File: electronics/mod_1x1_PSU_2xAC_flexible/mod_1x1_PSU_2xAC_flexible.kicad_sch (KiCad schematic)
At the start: 56 parts, among them J1 module_2x15_left_input, J2 module_2x15_right_input, J3 Jack-DC, J4 Jack-DC, J5 Conn_01x02, J6 Conn_01x02, U1 LM317, U2 LM317, U3 LM337, U4 LM78XX

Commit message: updated PCB with newer/different footprints
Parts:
- removed D3, D4: D, SquantorDiodes:SOD-123F-hand, symbol Device:D
- removed R1: R, SquantorRcl:R_1206, symbol Device:R
- D10, D12, D14: footprint SquantorDiodes:SOD-523_hand -> SquantorDiodes:SOD-323-nexperia-hand
- N1: value 202200917 -> 202201025
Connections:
- net AC1_NEUT is gone; now on net GND: F2.2
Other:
- moved on the sheet: C1

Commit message: small changes for producability and form and fit
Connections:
- net +5V: now also J1.10 (+5V), J1.9 (+5V)
- net V+A: now also J2.3 (+VA), J2.4 (+VA)
- net V-A: now also J1.5 (-VA), J1.6 (-VA)
- no-connect marks 26 -> 20
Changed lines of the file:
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@@
   )
   (no_connect (at 38.1 50.8))
-  (no_connect (at 20.32 27.94))
   (no_connect (at 38.1 38.1))
   (no_connect (at 38.1 55.88))
   (no_connect (at 38.1 43.18))
   (no_connect (at 20.32 99.06))
-  (no_connect (at 20.32 73.66))
-  (no_connect (at 38.1 27.94))
   (no_connect (at 38.1 48.26))
   (no_connect (at 20.32 86.36))
   (no_connect (at 20.32 88.9))
-  (no_connect (at 20.32 33.02))
   (no_connect (at 38.1 40.64))
   (no_connect (at 20.32 104.14))
-  (no_connect (at 38.1 73.66))
   (no_connect (at 38.1 53.34))
   (no_connect (at 20.32 96.52))
@@
   (no_connect (at 90.17 134.62))
   (no_connect (at 20.32 101.6))
-  (no_connect (at 38.1 33.02))
   (wire (pts (xy 114.3 81.28) (xy 114.3 78.74))
     (stroke (width 0) (type default))
@@
     (stroke (width 0) (type default))
   )
+  (wire (pts (xy 38.1 73.66) (xy 40.64 73.66))
+    (stroke (width 0) (type default))
+  )
   (wire (pts (xy 113.03 76.2) (xy 114.3 76.2))
     (stroke (width 0) (type default))
@@
     (stroke (width 0) (type default))
   )
+  (wire (pts (xy 17.78 27.94) (xy 20.32 27.94))
+    (stroke (width 0) (type default))
+  )
   (wire (pts (xy 66.04 73.66) (xy 66.04 76.2))
     (stroke (width 0) (type default))
@@
     (stroke (width 0) (type default))
   )
+  (wire (pts (xy 38.1 27.94) (xy 40.64 27.94))
+    (stroke (width 0) (type default))
+  )
   (wire (pts (xy 19.05 50.8) (xy 20.32 50.8))
     (stroke (width 0) (type default))
@@
     (stroke (width 0) (type default))
   )
+  (wire (pts (xy 17.78 73.66) (xy 20.32 73.66))
+    (stroke (width 0) (type default))
+  )
   (polyline (pts (xy 46.99 151.13) (xy 72.39 151.13))
     (stroke (width 0) (type default))
@@
     (stroke (width 0) (type default))
   )
+  (wire (pts (xy 17.78 33.02) (xy 20.32 33.02))
+    (stroke (width 0) (type default))
+  )
   (wire (pts (xy 39.37 83.82) (xy 39.37 78.74))
     (stroke (width 0) (type default))
@@
     (stroke (width 0) (type default))
   )
+  (wire (pts (xy 38.1 33.02) (xy 40.64 33.02))
+    (stroke (width 0) (type default))
+  )
   (wire (pts (xy 58.42 16.51) (xy 58.42 21.59))
     (stroke (width 0) (type default))
@@
     (effects (font (size 1.27 1.27)) (justify left bottom))
   )
+  (label "+5V" (at 40.64 33.02 0) (fields_autoplaced)
+    (effects (font (size 1.27 1.27)) (justify left bottom))
+  )
   (label "DC1n" (at 102.87 83.82 0) (fields_autoplaced)
     (effects (font (size 1.27 1.27)) (justify left bottom))
@@
     (effects (font (size 1.27 1.27)) (justify left bottom))
   )
+  (label "V+A" (at 17.78 73.66 180) (fields_autoplaced)
+    (effects (font (size 1.27 1.27)) (justify right bottom))
+  )
   (label "V-A" (at 102.87 86.36 0) (fields_autoplaced)
     (effects (font (size 1.27 1.27)) (justify left bottom))
@@
     (effects (font (size 1.27 1.27)) (justify right bottom))
   )
+  (label "V-A" (at 17.78 27.94 180) (fields_autoplaced)
+    (effects (font (size 1.27 1.27)) (justify right bottom))
+  )
   (label "V+A" (at 63.5 102.87 0) (fields_autoplaced)
     (effects (font (size 1.27 1.27)) (justify left bottom))
@@
     (effects (font (size 1.27 1.27)) (justify left bottom))
   )
+  (label "+5V" (at 17.78 33.02 180) (fields_autoplaced)
+    (effects (font (size 1.27 1.27)) (justify right bottom))
+  )
   (label "V+A" (at 40.64 25.4 0) (fields_autoplaced)
     (effects (font (size 1.27 1.27)) (justify left bottom))
   )
+  (label "V+A" (at 40.64 73.66 0) (fields_autoplaced)
+    (effects (font (size 1.27 1.27)) (justify left bottom))
+  )
   (label "V+A" (at 66.04 83.82 0) (fields_autoplaced)
     (effects (font (size 1.27 1.27)) (justify left bottom))
@@
     (effects (font (size 1.27 1.27)) (justify left bottom))
   )
+  (label "V-A" (at 40.64 27.94 0) (fields_autoplaced)
+    (effects (font (size 1.27 1.27)) (justify left bottom))
+  )

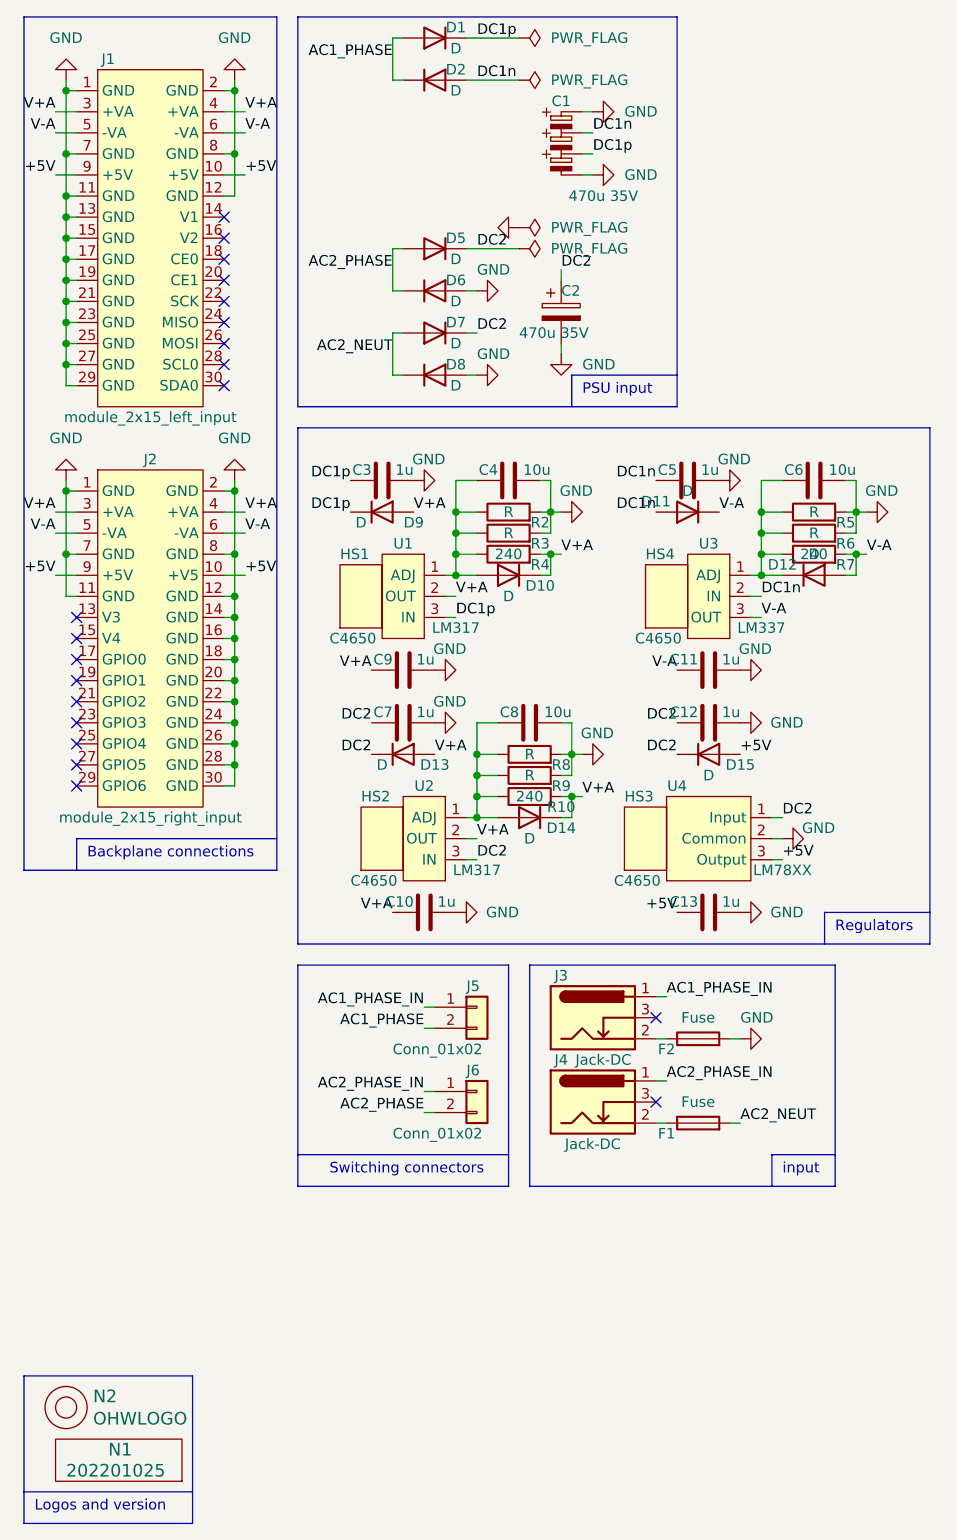
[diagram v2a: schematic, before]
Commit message: updated components and fixed warnings
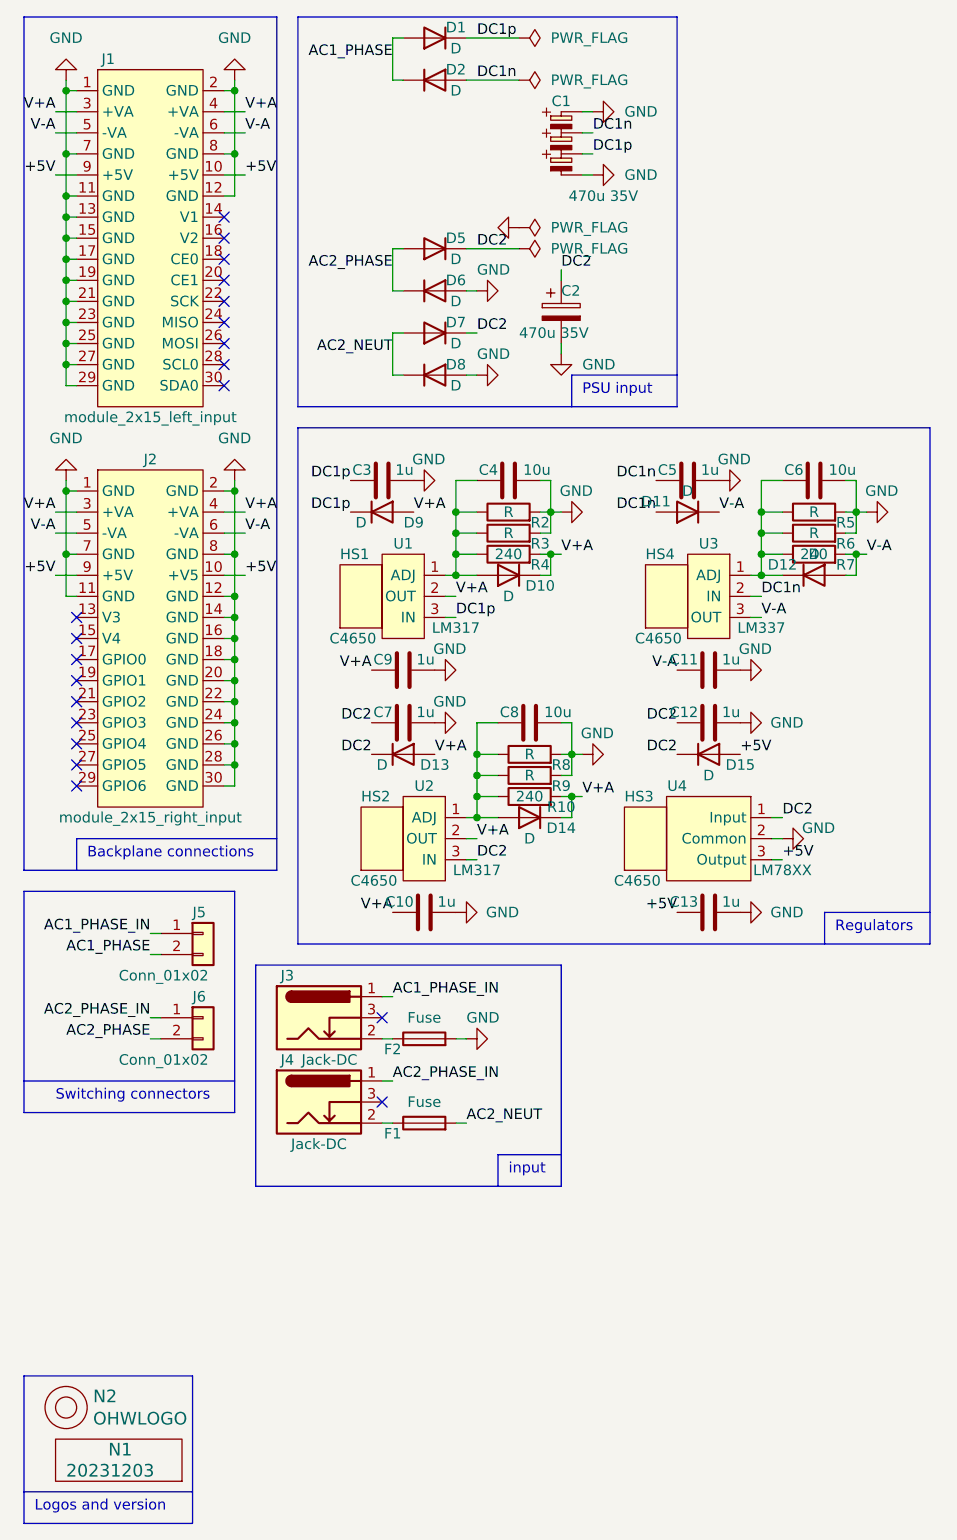
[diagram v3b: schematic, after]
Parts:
- N1: value 202201025 -> 20231203
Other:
- moved on the sheet: F1, F2, J3, J4, J5, J6

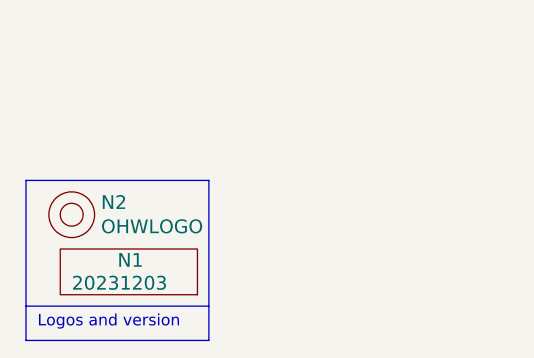
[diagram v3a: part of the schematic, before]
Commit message: imported aisler budget design rules, fixed all DRC errors resulting from that
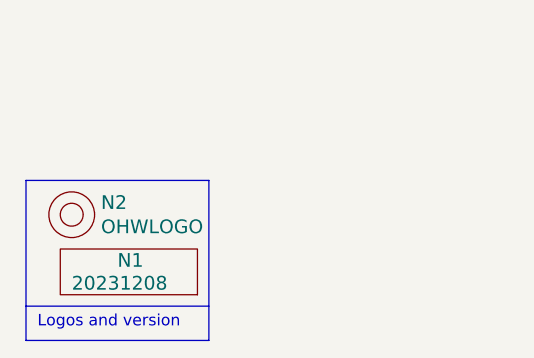
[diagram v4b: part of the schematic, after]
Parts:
- N1: value 20231203 -> 20231208
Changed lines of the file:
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@@
       (effects (font (size 1.524 1.524)) (justify left))
     )
-    (property "Value" "20231203" (at 19.05 189.23 0)
+    (property "Value" "20231208" (at 19.05 189.23 0)
       (effects (font (size 1.524 1.524)) (justify left))
     )

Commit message: WIP updated to new component libraries
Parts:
- C1: footprint SquantorRcl:Cx3-035-080-elco -> SquantorCapacitor:Cx3-035-080-elco
- C10, C11, C12, C13, C3, C4, C5, C6, C7, C8, C9: footprint SquantorRcl:C_0805+0603 -> SquantorCapacitor:C_0805+0603
- C2: footprint SquantorRcl:C-035-080-elco -> SquantorCapacitor:C-035-080-elco
- R10, R2, R3, R4, R5, R6, R7, R8, R9: footprint SquantorRcl:R_0805+0603 -> SquantorResistor:R_0805+0603
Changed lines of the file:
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@@
       (effects (font (size 1.27 1.27)) (justify left))
     )
-    (property "Footprint" "SquantorRcl:C_0805+0603" (at 113.03 68.8848 0)
+    (property "Footprint" "SquantorCapacitor:C_0805+0603" (at 113.03 68.8848 0)
       (effects (font (size 1.27 1.27)) hide)
     )
@@
       (effects (font (size 1.27 1.27)) (justify left))
     )
-    (property "Footprint" "SquantorRcl:C_0805+0603" (at 63.5 98.0948 0)
+    (property "Footprint" "SquantorCapacitor:C_0805+0603" (at 63.5 98.0948 0)
       (effects (font (size 1.27 1.27)) hide)
     )
@@
       (effects (font (size 1.27 1.27)) (justify left))
     )
-    (property "Footprint" "SquantorRcl:C_0805+0603" (at 100.33 120.9548 0)
+    (property "Footprint" "SquantorCapacitor:C_0805+0603" (at 100.33 120.9548 0)
       (effects (font (size 1.27 1.27)) hide)
     )
@@
       (effects (font (size 1.27 1.27)))
     )
-    (property "Footprint" "SquantorRcl:R_0805+0603" (at 72.39 77.978 90)
+    (property "Footprint" "SquantorResistor:R_0805+0603" (at 72.39 77.978 90)
       (effects (font (size 1.27 1.27)) hide)
     )
@@
       (effects (font (size 1.27 1.27)))
     )
-    (property "Footprint" "SquantorRcl:R_0805+0603" (at 72.39 80.518 90)
+    (property "Footprint" "SquantorResistor:R_0805+0603" (at 72.39 80.518 90)
       (effects (font (size 1.27 1.27)) hide)
     )
@@
       (effects (font (size 1.27 1.27)))
     )
-    (property "Footprint" "SquantorRcl:R_0805+0603" (at 74.93 109.728 90)
+    (property "Footprint" "SquantorResistor:R_0805+0603" (at 74.93 109.728 90)
       (effects (font (size 1.27 1.27)) hide)
     )
@@
       (effects (font (size 1.27 1.27)) (justify left))
     )
-    (property "Footprint" "SquantorRcl:C_0805+0603" (at 66.04 120.9548 0)
+    (property "Footprint" "SquantorCapacitor:C_0805+0603" (at 66.04 120.9548 0)
       (effects (font (size 1.27 1.27)) hide)
     )
@@
       (effects (font (size 1.27 1.27)) (justify left))
     )
-    (property "Footprint" "SquantorRcl:C_0805+0603" (at 60.96 68.8848 0)
+    (property "Footprint" "SquantorCapacitor:C_0805+0603" (at 60.96 68.8848 0)
       (effects (font (size 1.27 1.27)) hide)
     )
@@
       (effects (font (size 1.27 1.27)) (justify left))
     )
-    (property "Footprint" "SquantorRcl:C_0805+0603" (at 100.33 91.7448 0)
+    (property "Footprint" "SquantorCapacitor:C_0805+0603" (at 100.33 91.7448 0)
       (effects (font (size 1.27 1.27)) hide)
     )
@@
       (effects (font (size 1.27 1.27)) (justify left))
     )
-    (property "Footprint" "SquantorRcl:C_0805+0603" (at 76.2 68.8848 0)
+    (property "Footprint" "SquantorCapacitor:C_0805+0603" (at 76.2 68.8848 0)
       (effects (font (size 1.27 1.27)) hide)
     )
@@
       (effects (font (size 1.27 1.27)))
     )
-    (property "Footprint" "SquantorRcl:R_0805+0603" (at 74.93 104.648 90)
+    (property "Footprint" "SquantorResistor:R_0805+0603" (at 74.93 104.648 90)
       (effects (font (size 1.27 1.27)) hide)
     )
@@
       (effects (font (size 1.27 1.27)) (justify left))
     )
-    (property "Footprint" "SquantorRcl:C_0805+0603" (at 97.79 68.8848 0)
+    (property "Footprint" "SquantorCapacitor:C_0805+0603" (at 97.79 68.8848 0)
       (effects (font (size 1.27 1.27)) hide)
     )
@@
       (effects (font (size 1.27 1.27)))
     )
-    (property "Footprint" "SquantorRcl:R_0805+0603" (at 109.22 80.518 90)
+    (property "Footprint" "SquantorResistor:R_0805+0603" (at 109.22 80.518 90)
       (effects (font (size 1.27 1.27)) hide)
     )
@@
       (effects (font (size 1.27 1.27)))
     )
-    (property "Footprint" "SquantorRcl:R_0805+0603" (at 74.93 107.188 90)
+    (property "Footprint" "SquantorResistor:R_0805+0603" (at 74.93 107.188 90)
       (effects (font (size 1.27 1.27)) hide)
     )
@@
       (effects (font (size 1.27 1.27)) (justify left))
     )
-    (property "Footprint" "SquantorRcl:C_0805+0603" (at 100.33 98.0948 0)
+    (property "Footprint" "SquantorCapacitor:C_0805+0603" (at 100.33 98.0948 0)
       (effects (font (size 1.27 1.27)) hide)
     )
@@
       (effects (font (size 1.27 1.27)))
     )
-    (property "Footprint" "SquantorRcl:R_0805+0603" (at 72.39 75.438 90)
+    (property "Footprint" "SquantorResistor:R_0805+0603" (at 72.39 75.438 90)
       (effects (font (size 1.27 1.27)) hide)
     )
@@
       (effects (font (size 1.27 1.27)))
     )
-    (property "Footprint" "SquantorRcl:R_0805+0603" (at 109.22 77.978 90)
+    (property "Footprint" "SquantorResistor:R_0805+0603" (at 109.22 77.978 90)
       (effects (font (size 1.27 1.27)) hide)
     )
@@
       (effects (font (size 1.27 1.27)) (justify left))
     )
-    (property "Footprint" "SquantorRcl:C-035-080-elco" (at 79.7052 53.34 0)
+    (property "Footprint" "SquantorCapacitor:C-035-080-elco" (at 79.7052 53.34 0)
       (effects (font (size 1.27 1.27)) hide)
     )
@@
       (effects (font (size 1.27 1.27)) (justify left))
     )
-    (property "Footprint" "SquantorRcl:C_0805+0603" (at 78.74 98.0948 0)
+    (property "Footprint" "SquantorCapacitor:C_0805+0603" (at 78.74 98.0948 0)
       (effects (font (size 1.27 1.27)) hide)
     )
@@
       (effects (font (size 1.27 1.27)))
     )
-    (property "Footprint" "SquantorRcl:Cx3-035-080-elco" (at 78.74 29.21 0)
+    (property "Footprint" "SquantorCapacitor:Cx3-035-080-elco" (at 78.74 29.21 0)
       (effects (font (size 1.27 1.27)) hide)
     )
@@
       (effects (font (size 1.27 1.27)))
     )
-    (property "Footprint" "SquantorRcl:R_0805+0603" (at 109.22 75.438 90)
+    (property "Footprint" "SquantorResistor:R_0805+0603" (at 109.22 75.438 90)
       (effects (font (size 1.27 1.27)) hide)
     )
@@
       (effects (font (size 1.27 1.27)) (justify left))
     )
-    (property "Footprint" "SquantorRcl:C_0805+0603" (at 63.5 91.7448 0)
-      (effects (font (size 1.27 1.27)) hide)
-    )
+    (property "Footprint" "SquantorCapacitor:C_0805+0603" (at 63.5 91.7448 0)
+      (effects (font (size 1.27 1.27)) hide)
+    )
